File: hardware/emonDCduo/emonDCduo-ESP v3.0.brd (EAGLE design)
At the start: 16 x 2 mm, 87 parts, among them IC1 ACS758LCB-050B-PFF-T, IC2 ACS758LCB-050B-PFF-T, IC3 LM358D, P1 B4B-PH-K, Y1 32Khz

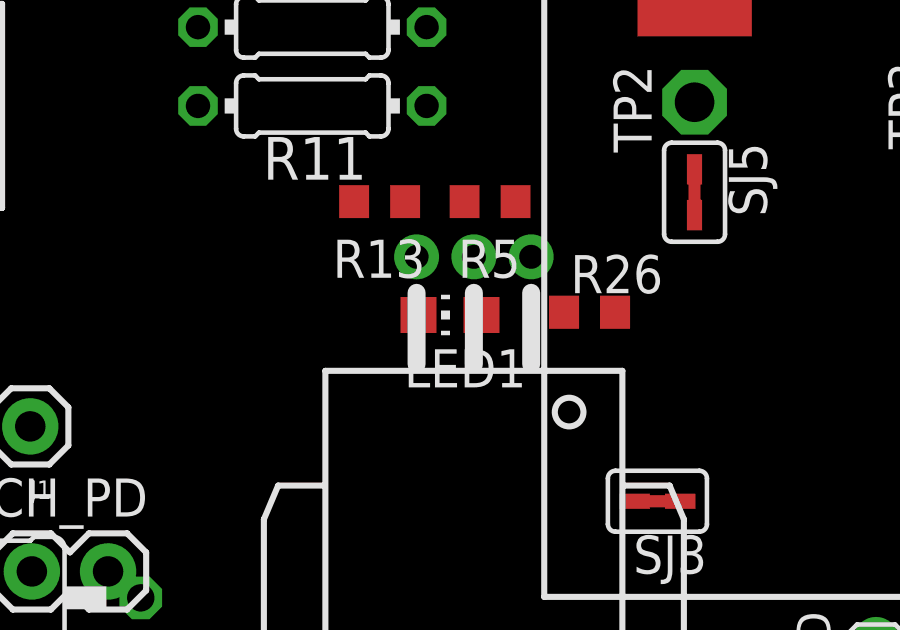
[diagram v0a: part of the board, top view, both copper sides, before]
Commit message: starting v3.0 and ASC770 breakout
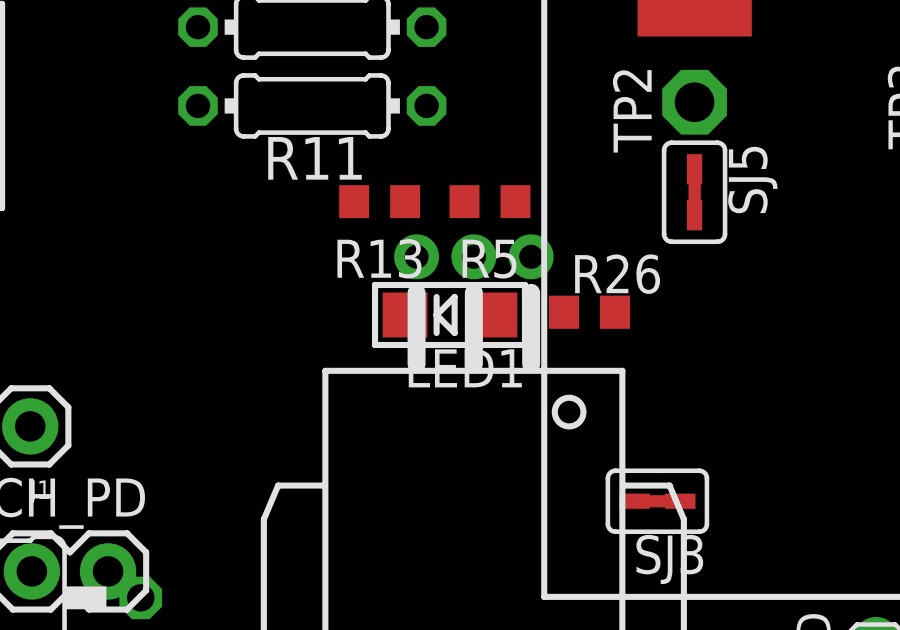
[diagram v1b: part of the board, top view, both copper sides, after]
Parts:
- LED1: device led:CHIP-LED0805 -> microbuilder:CHIPLED_1206
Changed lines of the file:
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@@
 <attribute name="VALUE" x="80.365" y="38.095" size="1.27" layer="27"/>
 </element>
-<element name="LED1" library="led" library_urn="urn:adsk.eagle:library:259" package="CHIP-LED0805" package3d_urn="urn:adsk.eagle:package:15818/2" value="" x="76.348" y="39.908" smashed="yes" rot="R90">
+<element name="LED1" library="microbuilder" package="CHIPLED_1206" value="" x="76.348" y="39.908" smashed="yes" rot="R90">
 <attribute name="NAME" x="78.888" y="38.765" size="1.27" layer="25" rot="R180"/>
 <attribute name="VALUE" x="77.618" y="42.448" size="1.27" layer="27" rot="R180"/>
@@
 <wire x1="67.948" y1="46.877" x2="71.1664375" y2="55.17290625" width="0" layer="19" extent="1-1"/>
 <wire x1="73.152" y1="43.688" x2="67.948" y2="46.877" width="0" layer="19" extent="1-1"/>
-<wire x1="75.298" y1="39.908" x2="73.152" y2="43.688" width="0" layer="19" extent="1-1"/>
-<wire x1="77.143890625" y1="41.847" x2="75.298" y2="39.908" width="0" layer="19" extent="1-1"/>
+<wire x1="74.852" y1="39.908" x2="73.152" y2="43.688" width="0" layer="19" extent="1-1"/>
+<wire x1="77.143890625" y1="41.847" x2="74.852" y2="39.908" width="0" layer="19" extent="1-1"/>
 <wire x1="58.018" y1="48.628" x2="67.948" y2="46.877" width="0" layer="19" extent="1-1"/>
 <wire x1="58.018" y1="45.128" x2="58.018" y2="48.628" width="0" layer="19" extent="1-1"/>
@@
 <wire x1="5.323665625" y1="62.83694375" x2="13.623665625" y2="62.83694375" width="0" layer="19" extent="1-1"/>
 <wire x1="15.78" y1="35.916" x2="26.343890625" y2="41.847" width="0" layer="19" extent="1-1"/>
-<wire x1="64.95" y1="31.36" x2="75.298" y2="39.908" width="0" layer="19" extent="1-1"/>
+<wire x1="64.95" y1="31.36" x2="74.852" y2="39.908" width="0" layer="19" extent="1-1"/>
 <wire x1="59.355878125" y1="62.322759375" x2="58.018" y2="48.628" width="0" layer="19" extent="1-1"/>
 <wire x1="58.399365625" y1="72.15505625" x2="59.355878125" y2="62.322759375" width="0" layer="19" extent="1-1"/>
@@
 <wire x1="48.495828125" y1="65.044175" x2="59.355878125" y2="62.322759375" width="0" layer="19" extent="1-1"/>
 <wire x1="39.38" y1="69.723" x2="48.495828125" y2="65.044175" width="0" layer="19" extent="1-1"/>
-<wire x1="82.870265625" y1="27.122453125" x2="75.298" y2="39.908" width="0" layer="19" extent="1-1"/>
+<wire x1="82.870265625" y1="27.122453125" x2="74.852" y2="39.908" width="0" layer="19" extent="1-1"/>
 <wire x1="90.551" y1="28.321" x2="82.870265625" y2="27.122453125" width="0" layer="19" extent="1-1"/>
 <wire x1="91.23954375" y1="21.26408125" x2="90.551" y2="28.321" width="0" layer="19" extent="1-1"/>
@@
 <contactref element="R26" pad="1"/>
 <contactref element="LED1" pad="A"/>
-<wire x1="77.398" y1="39.908" x2="80.15" y2="40" width="0" layer="19" extent="1-1"/>
+<wire x1="77.844" y1="39.908" x2="80.15" y2="40" width="0" layer="19" extent="1-1"/>
 </signal>
 <signal name="N$24">
